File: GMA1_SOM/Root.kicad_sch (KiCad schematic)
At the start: 2 parts, among them J1 USB4105-GF-A, J2 SODIMM-200_Split

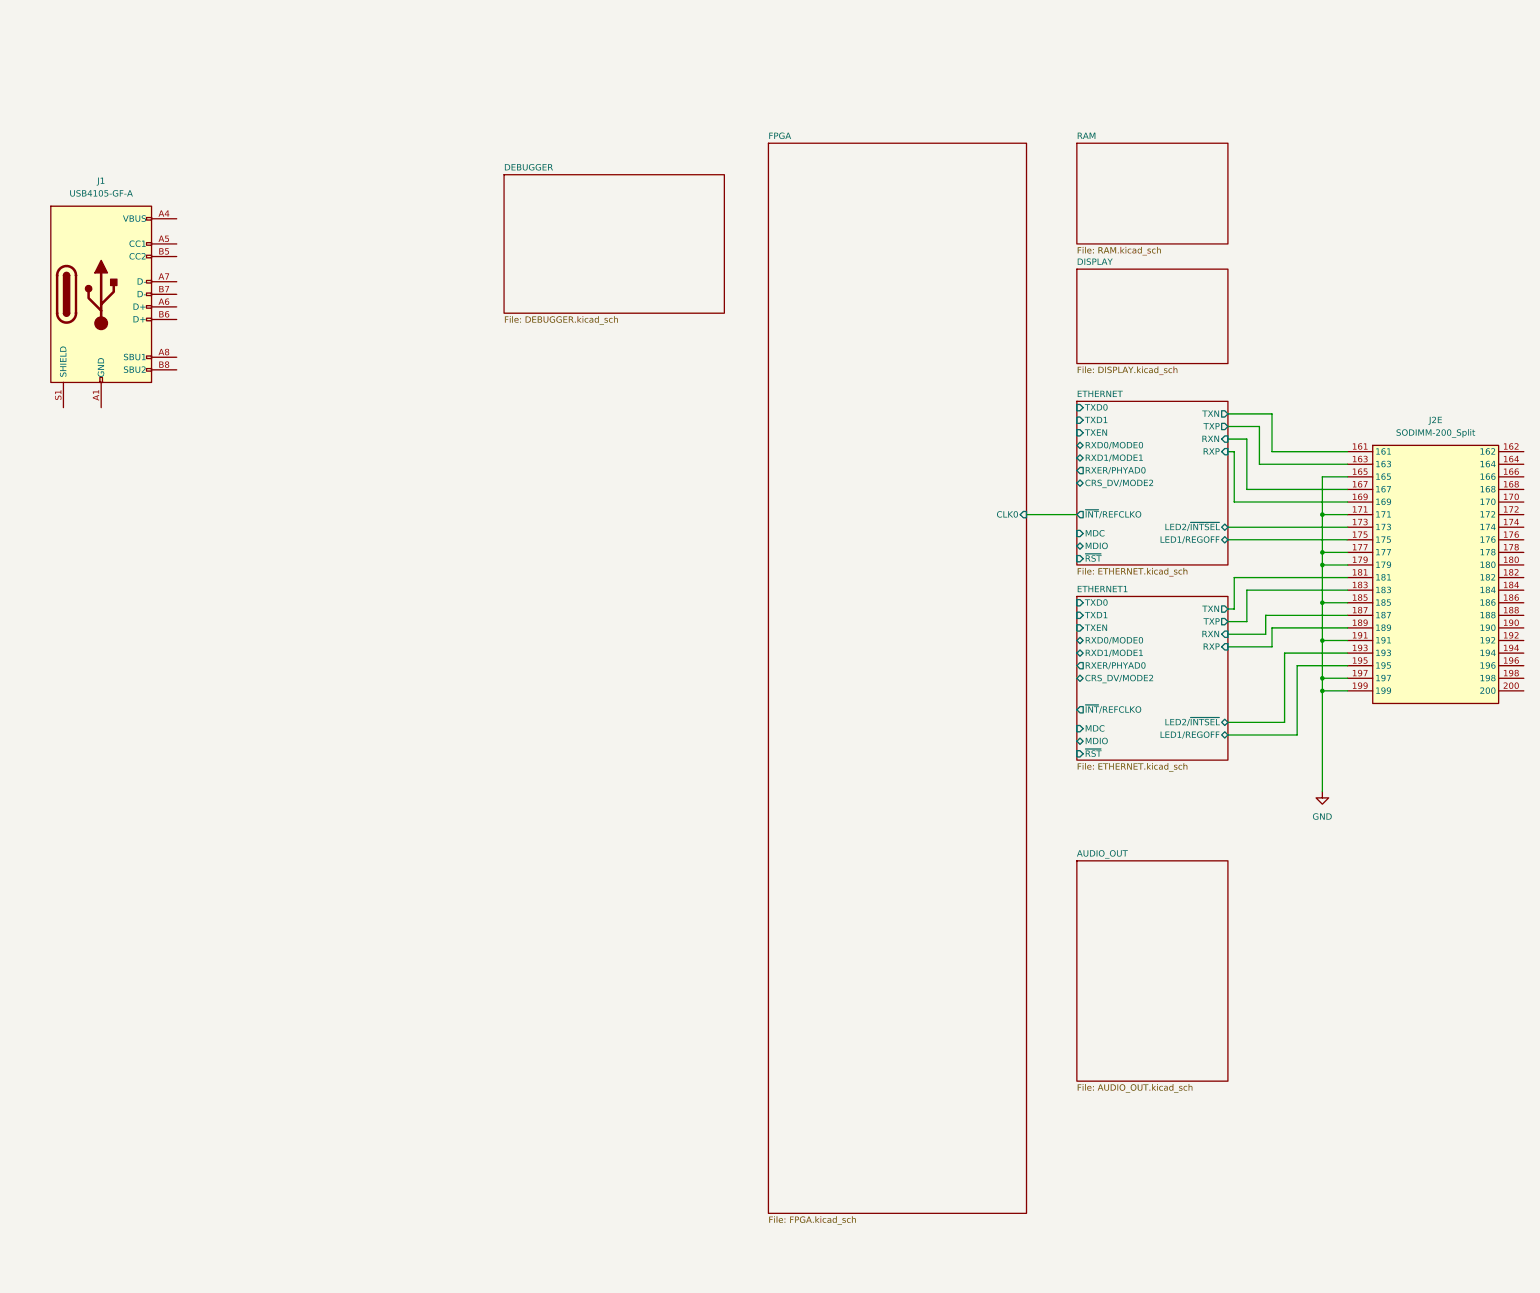
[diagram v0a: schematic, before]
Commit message: add display and ram
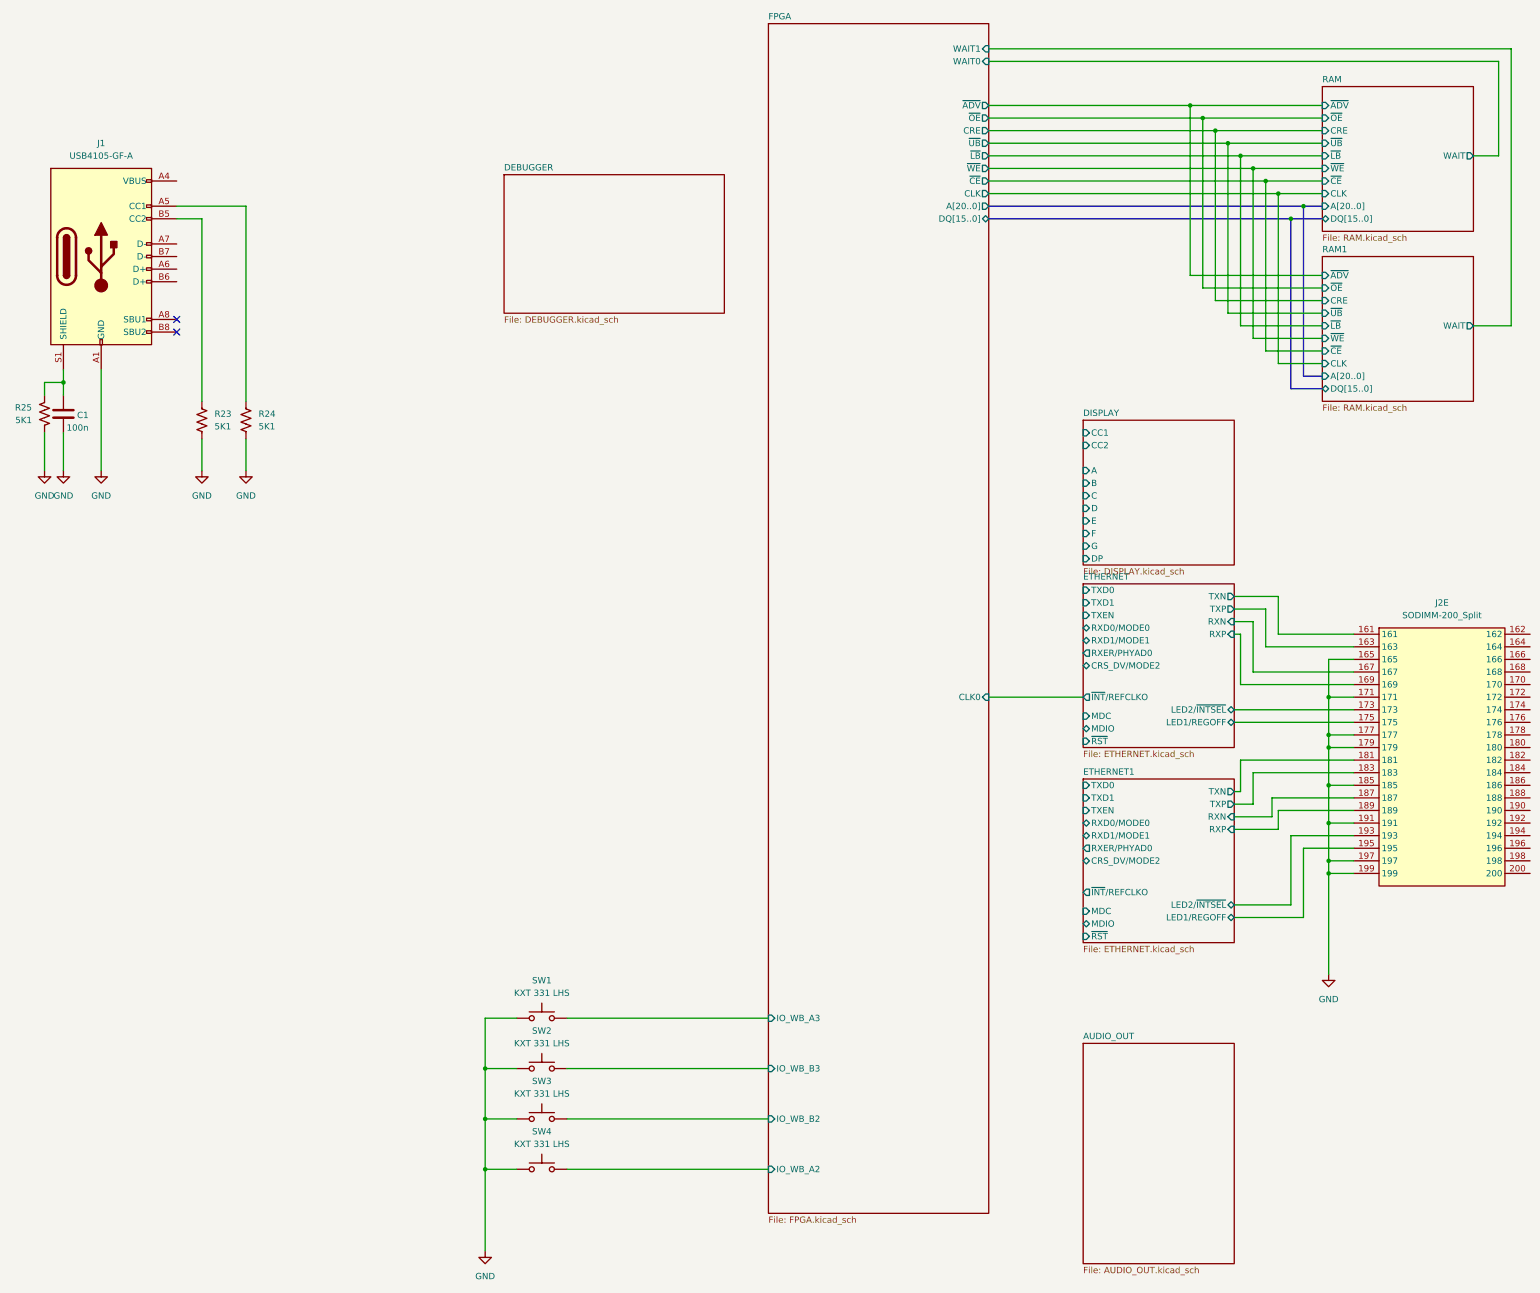
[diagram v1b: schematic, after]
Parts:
- added C1: 100n, symbol Device:C
- added R23, R24, R25: 5K1, symbol Device:R_US
- added SW1, SW2, SW3, SW4: KXT 331 LHS, Button_Switch_SMD:SW_SPST_CK_KXT3, symbol Switch:SW_Push
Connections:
- net GND: now also J1.A1 (GND), J1.A12 (GND), J1.B1 (GND), J1.B12 (GND), C1.2, R23.2, R24.2, R25.2, SW1.1, SW2.1, SW3.1, SW4.1
- net at J1.A5 (CC1): now also R24.1
- net at J1.B5 (CC2): now also R23.1
- net at J1.S1 (SHIELD): now also C1.1, R25.1
- new net FPGA/IO_WB_A2: SW4.2
- new net FPGA/IO_WB_A3: SW1.2
- new net FPGA/IO_WB_B2: SW3.2
- new net FPGA/IO_WB_B3: SW2.2
- no-connect marks 0 -> 2
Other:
- added sheet RAM1 (RAM.kicad_sch)
- sheet DISPLAY ports: added A, B, C, CC1, CC2, D, DP, E, F, G; removed none
- sheet FPGA ports: added A[20..0], CLK, CRE, DQ[15..0], IO_WB_A2, IO_WB_A3, IO_WB_B2, IO_WB_B3, WAIT0, WAIT1, ~{ADV}, ~{CE}, ~{LB}, ~{OE}, ~{UB}, ~{WE}; removed none
- sheet RAM ports: added A[20..0], CLK, CRE, DQ[15..0], WAIT, ~{ADV}, ~{CE}, ~{LB}, ~{OE}, ~{UB}, ~{WE}; removed none
- moved on the sheet: J1, J2E
